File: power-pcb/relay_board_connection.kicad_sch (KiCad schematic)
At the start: 17 parts, among them J5 RA25S

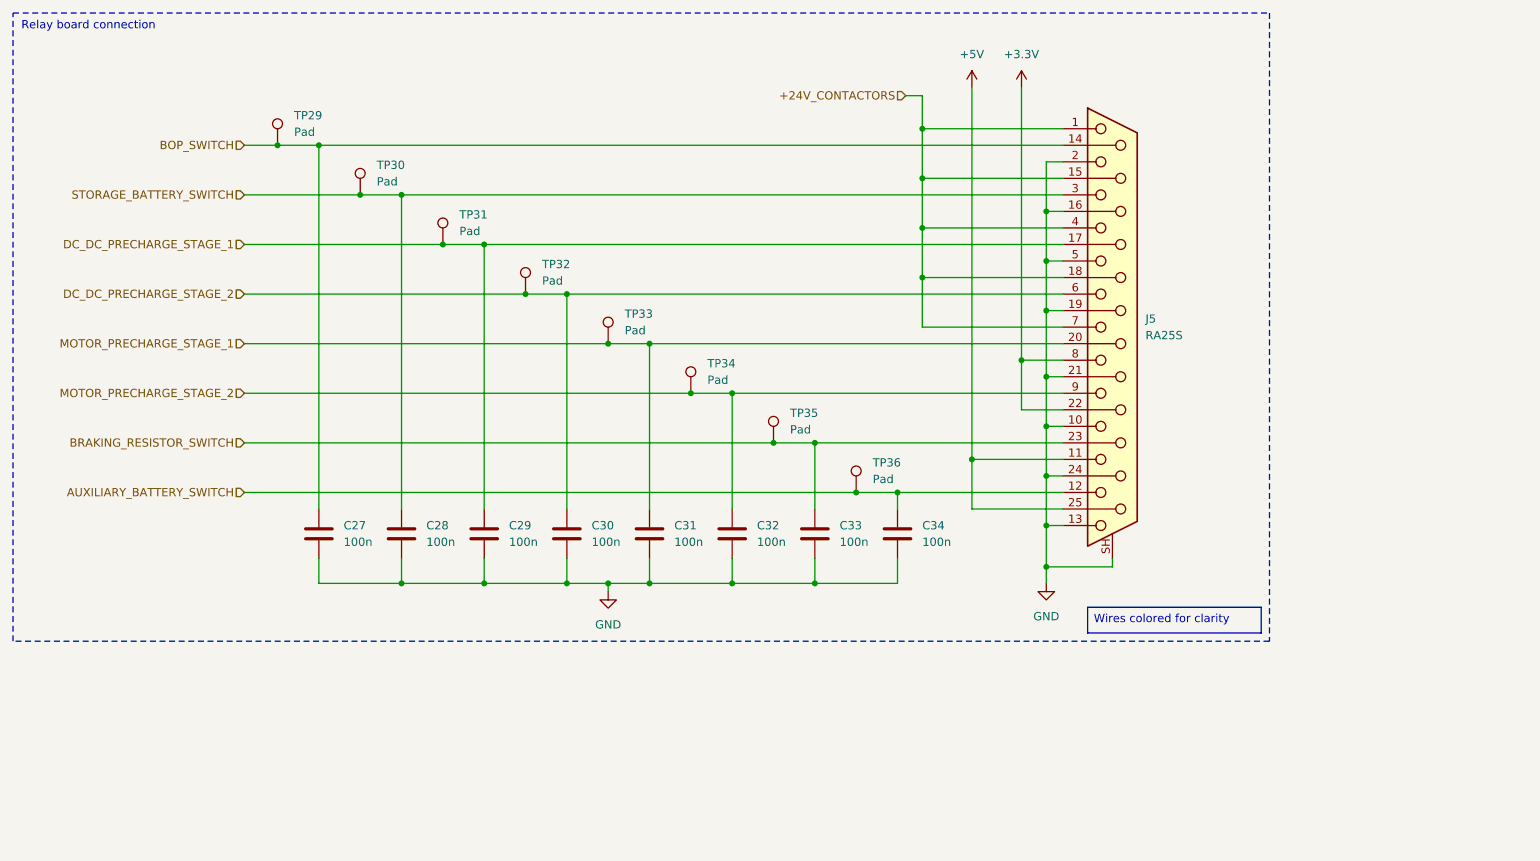
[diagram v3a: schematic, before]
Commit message: power-pcb: fix schematic after review
- Add footprint for resitive load for the RECOM
- Add Opamps when useful
- Add capacitor and change some footprint sizes
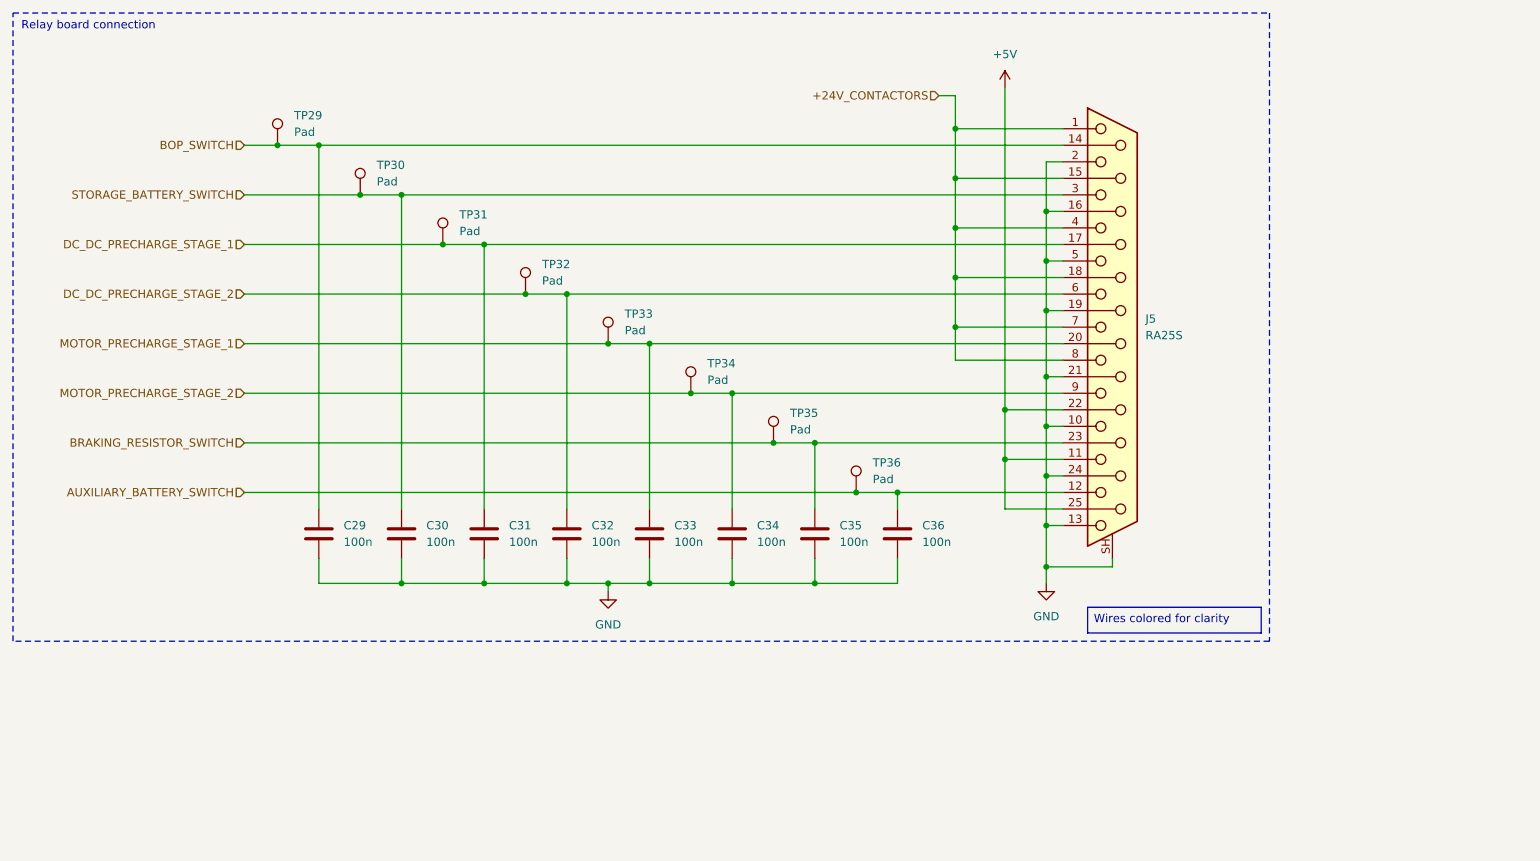
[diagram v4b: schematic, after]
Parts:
- C29: renamed from C27; footprint Capacitor_SMD:C_0603_1608Metric_Pad1.08x0.95mm_HandSolder -> Capacitor_SMD:C_0402_1005Metric_Pad0.74x0.62mm_HandSolder; JLCPCB C14663 -> C307331
- C30: renamed from C28; footprint Capacitor_SMD:C_0603_1608Metric_Pad1.08x0.95mm_HandSolder -> Capacitor_SMD:C_0402_1005Metric_Pad0.74x0.62mm_HandSolder; JLCPCB C14663 -> C307331
- C31: renamed from C29; footprint Capacitor_SMD:C_0603_1608Metric_Pad1.08x0.95mm_HandSolder -> Capacitor_SMD:C_0402_1005Metric_Pad0.74x0.62mm_HandSolder; JLCPCB C14663 -> C307331
- C32: renamed from C30; footprint Capacitor_SMD:C_0603_1608Metric_Pad1.08x0.95mm_HandSolder -> Capacitor_SMD:C_0402_1005Metric_Pad0.74x0.62mm_HandSolder; JLCPCB C14663 -> C307331
- C33: renamed from C31; footprint Capacitor_SMD:C_0603_1608Metric_Pad1.08x0.95mm_HandSolder -> Capacitor_SMD:C_0402_1005Metric_Pad0.74x0.62mm_HandSolder; JLCPCB C14663 -> C307331
- C34: renamed from C32; footprint Capacitor_SMD:C_0603_1608Metric_Pad1.08x0.95mm_HandSolder -> Capacitor_SMD:C_0402_1005Metric_Pad0.74x0.62mm_HandSolder; JLCPCB C14663 -> C307331
- C35: renamed from C33; footprint Capacitor_SMD:C_0603_1608Metric_Pad1.08x0.95mm_HandSolder -> Capacitor_SMD:C_0402_1005Metric_Pad0.74x0.62mm_HandSolder; JLCPCB C14663 -> C307331
- C36: renamed from C34; footprint Capacitor_SMD:C_0603_1608Metric_Pad1.08x0.95mm_HandSolder -> Capacitor_SMD:C_0402_1005Metric_Pad0.74x0.62mm_HandSolder; JLCPCB C14663 -> C307331
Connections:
- net +24V_CONTACTORS: now also J5.8
- net +5V: now also J5.22 (P22)
- removed net +3.3V: J5.22 (P22), J5.8
